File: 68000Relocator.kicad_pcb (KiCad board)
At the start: 2 copper layers, 97.4 x 94.7 mm, 3 parts, among them P99 OSHW_LOGO, U1 68000D, U2 68000D

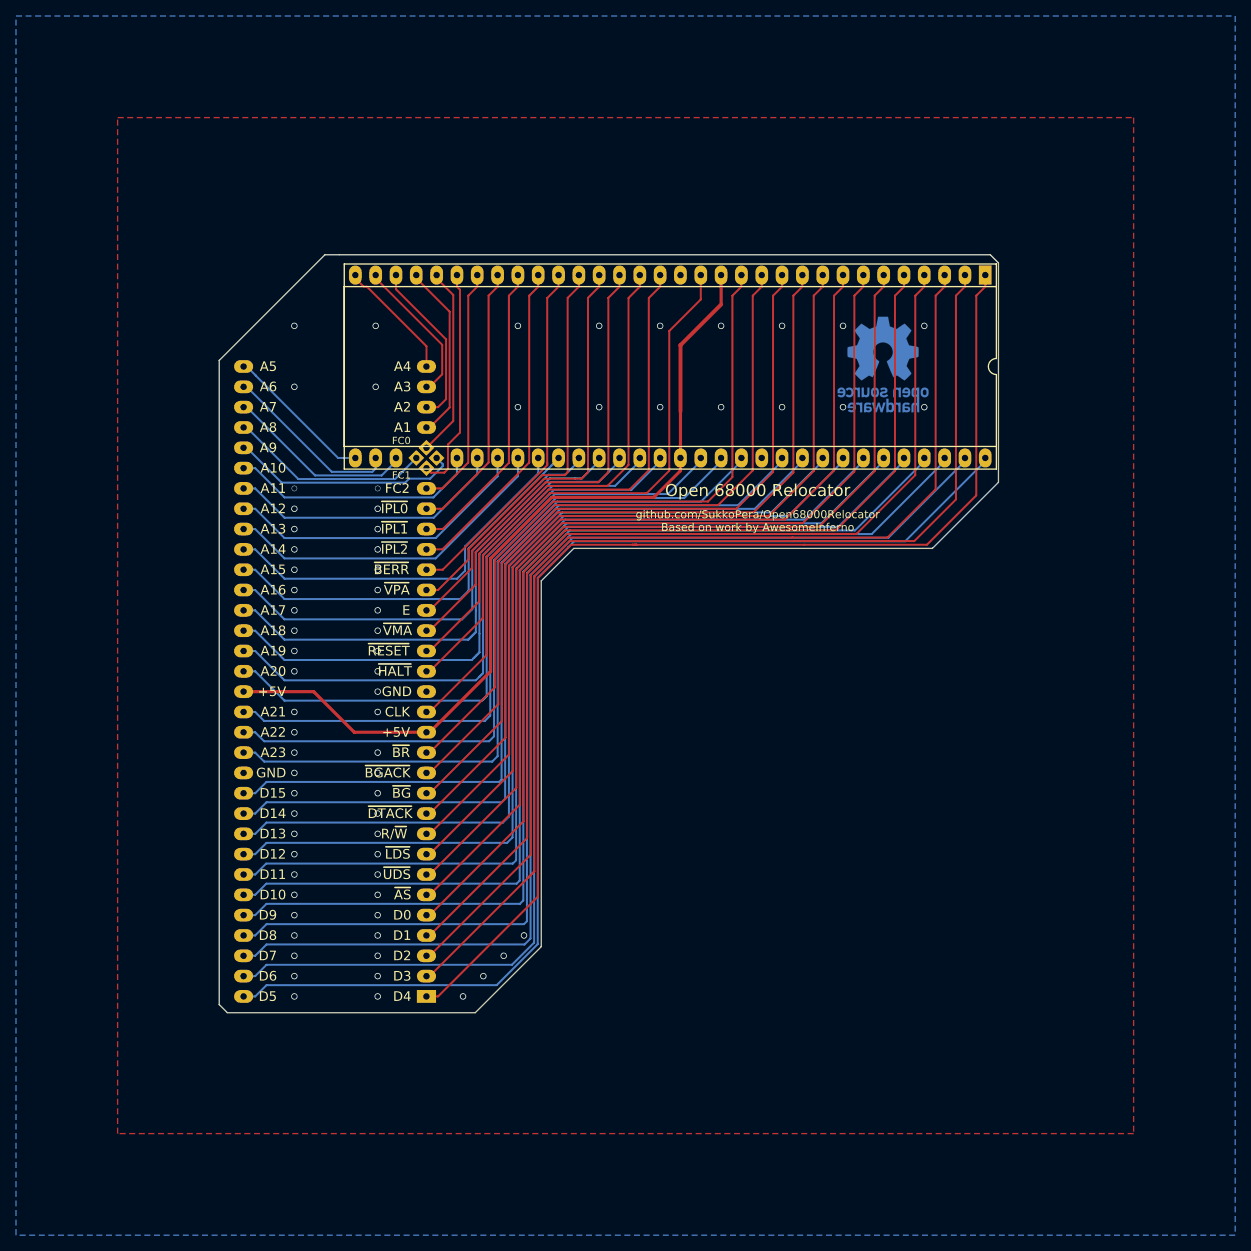
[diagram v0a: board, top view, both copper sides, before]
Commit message: My spin on SukkoPera's design
Added a hole for the capacitor in rev 6 and 8, plus a few other minor
tweaks.
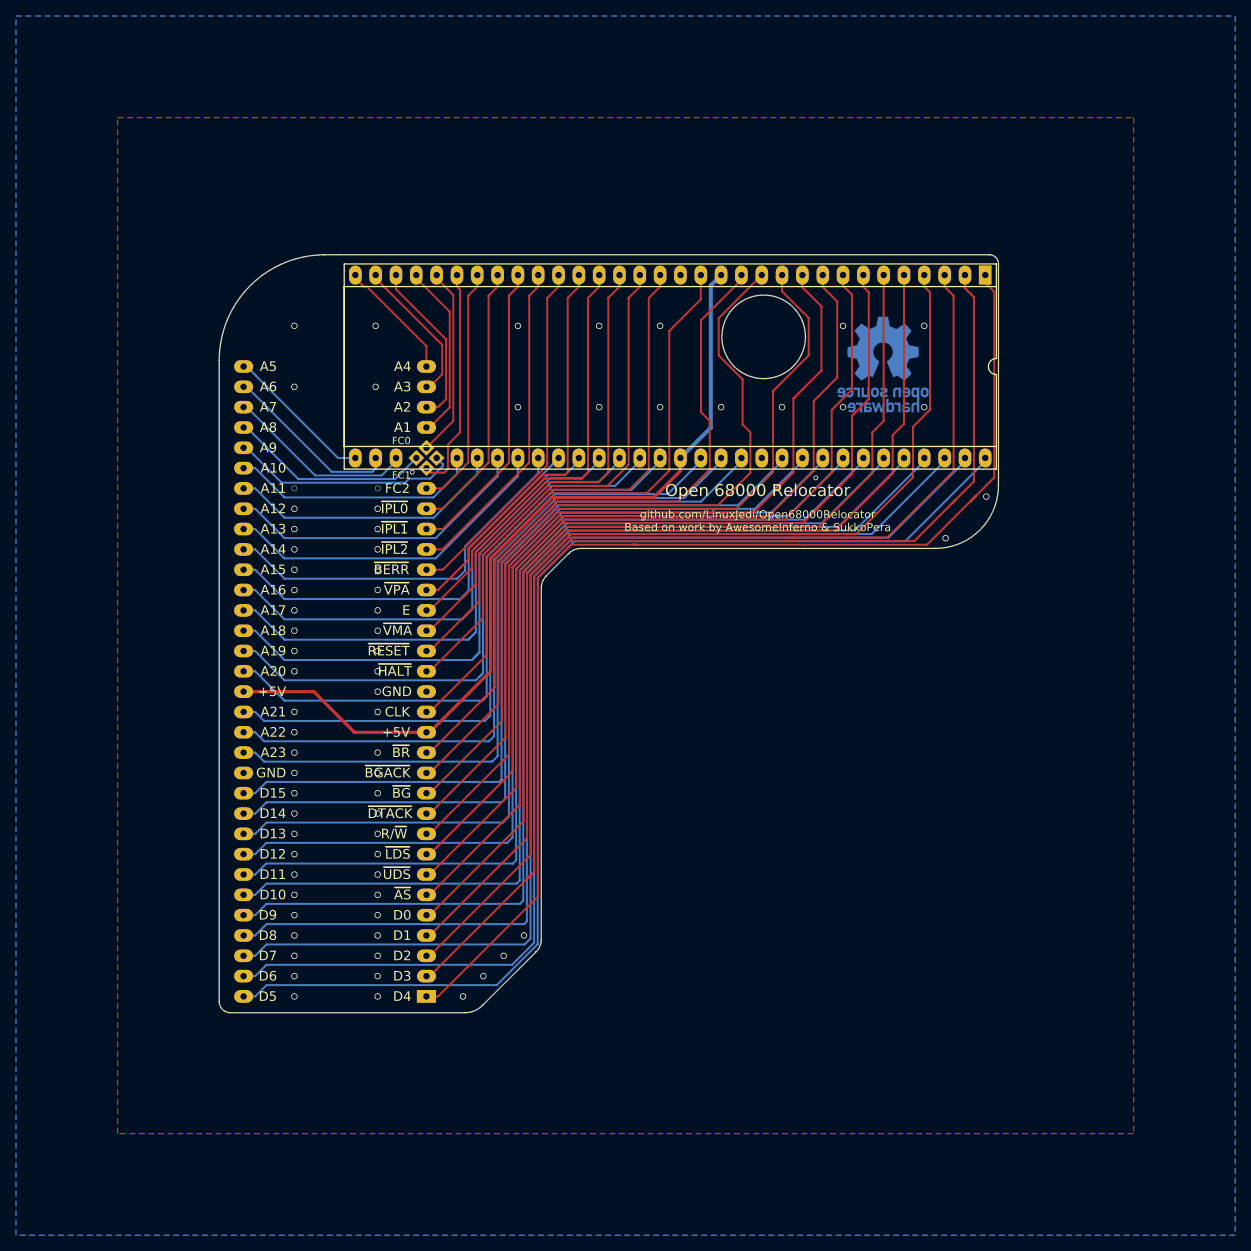
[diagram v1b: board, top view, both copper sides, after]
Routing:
- net /BGACK: track 91.8 -> 95.1 mm
- net /BG: track 97.3 -> 100.1 mm
- net /DTACK: track 101.3 -> 103.3 mm
- net /D4: track 147.2 -> 149.1 mm
- net /D2: track 135.5 -> 137.2 mm
- net /D3: track 142.0 -> 143.5 mm
- net /R/W: track 105.9 -> 107.4 mm
- net /BR: track 87.5 -> 86.2 mm
- net /LDS: track 110.6 -> 111.5 mm
- net /D1: track 130.1 -> 130.7 mm
- net /UDS: track 115.4 -> 116.0 mm
- net GND: vias 72 -> 74
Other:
- outline, holes or cut-outs redrawn
- board text added: "V1a"
- board text added: "github.com/LinuxJedi/Open68000Relocator Based on work by AwesomeInferno & SukkoPera"
- board text removed: "V1"
- board text removed: "github.com/SukkoPera/Open68000Relocator Based on work by AwesomeInferno"
